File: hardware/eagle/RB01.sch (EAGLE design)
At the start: 10 parts, among them J1 CON_TERMINAL_BLOCK_03-5MM, J2 CON_TERMINAL_BLOCK_02-5MM, K1 JS-M1A-12V-5, Q1 BC547

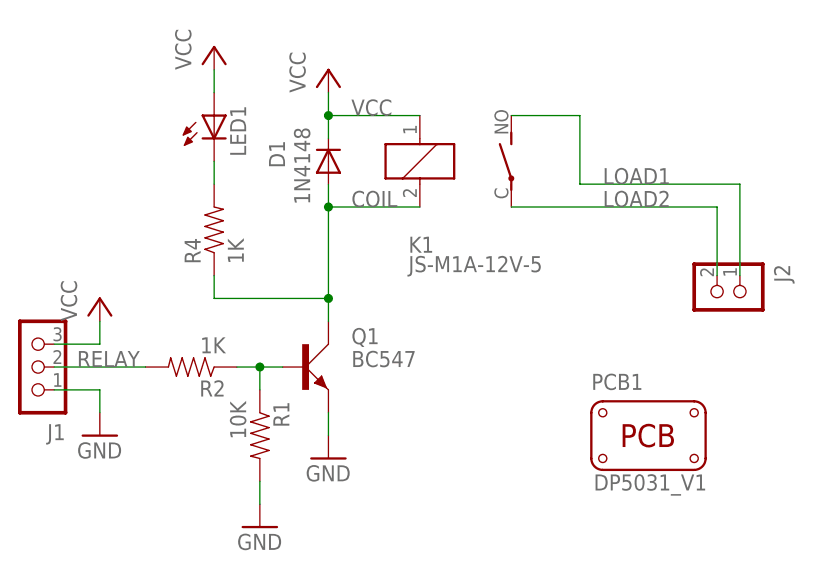
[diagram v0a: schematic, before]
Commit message: BC337s instead of BC546s
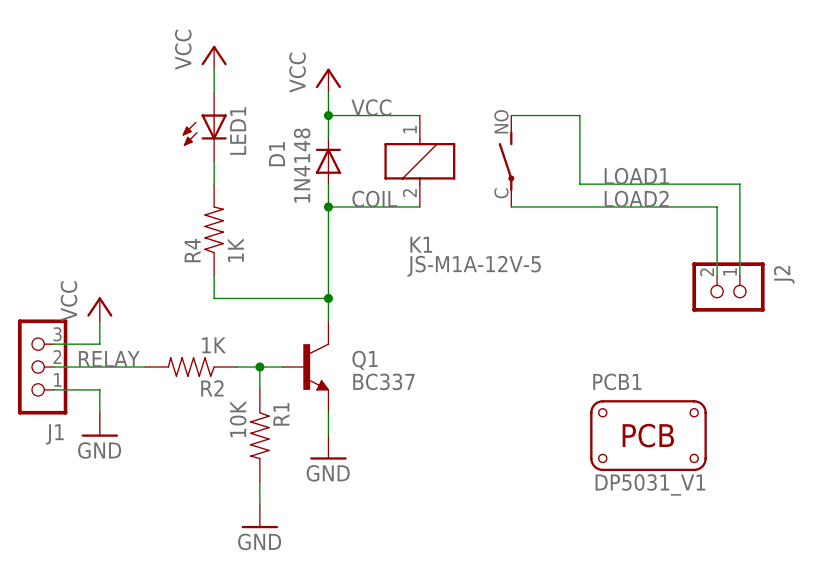
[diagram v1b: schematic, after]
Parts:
- Q1: value BC547 -> BC337; device transistor-small-signal:BC547 -> transistor:BC337
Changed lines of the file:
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@@
 <part name="J1" library="dp_devices" deviceset="CON_TERMINAL_BLOCK_03" device="-5MM"/>
 <part name="J2" library="dp_devices" deviceset="CON_TERMINAL_BLOCK_02" device="-5MM"/>
-<part name="Q1" library="transistor-small-signal" deviceset="BC547" device=""/>
+<part name="Q1" library="transistor" deviceset="BC337" device=""/>
 <part name="K1" library="relay" deviceset="JS-M1A*" device="" technology="-12V-5"/>
 <part name="PCB1" library="dp_devices" deviceset="PCB_DP_RECTANGLE" device="-31X50"/>
@@
 <instance part="J1" gate="CON" x="96.52" y="86.36" rot="R180"/>
 <instance part="J2" gate="CON" x="172.72" y="96.52" rot="R270"/>
-<instance part="Q1" gate="1" x="124.46" y="86.36"/>
+<instance part="Q1" gate="G$1" x="124.46" y="86.36" smashed="yes">
+<attribute name="NAME" x="129.54" y="86.36" size="1.778" layer="95"/>
+<attribute name="VALUE" x="129.54" y="83.82" size="1.778" layer="96"/>
+</instance>
 <instance part="K1" gate="1" x="137.16" y="109.22" smashed="yes">
 <attribute name="VALUE" x="135.89" y="96.901" size="1.778" layer="96"/>
@@
 <segment>
 <pinref part="GND1" gate="1" pin="GND"/>
-<pinref part="Q1" gate="1" pin="E"/>
+<pinref part="Q1" gate="G$1" pin="E"/>
 <wire x1="127" y1="78.74" x2="127" y2="81.28" width="0.1524" layer="91"/>
 </segment>
@@
 <pinref part="R2" gate="G$1" pin="1"/>
 <pinref part="R1" gate="G$1" pin="1"/>
-<pinref part="Q1" gate="1" pin="B"/>
+<pinref part="Q1" gate="G$1" pin="B"/>
 <wire x1="121.92" y1="86.36" x2="119.38" y2="86.36" width="0.1524" layer="91"/>
 <junction x="119.38" y="86.36"/>
@@
 <pinref part="D1" gate="G$1" pin="A"/>
 <pinref part="R4" gate="G$1" pin="1"/>
-<pinref part="Q1" gate="1" pin="C"/>
+<pinref part="Q1" gate="G$1" pin="C"/>
 <wire x1="127" y1="91.44" x2="127" y2="93.98" width="0.1524" layer="91"/>
 <junction x="127" y="93.98"/>

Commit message: JS-M1 relay package
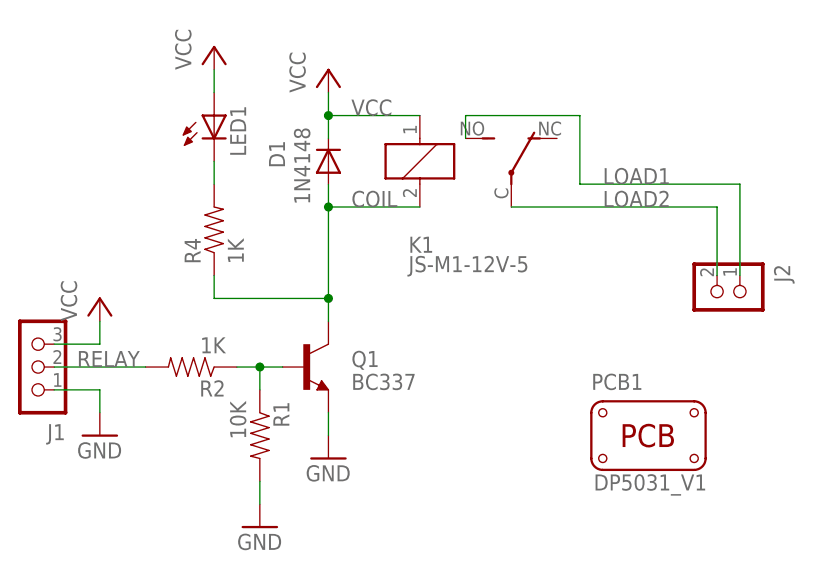
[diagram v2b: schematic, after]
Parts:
- K1: value JS-M1A-12V-5 -> JS-M1-12V-5; device relay:JS-M1A-12V-5 -> relay:JS-M1-12V-5; MF (none) -> FARNELL; MPN (none) -> JSM1-12V-5; OC_FARNELL (none) -> 910351; OC_NEWARK (none) -> 14J1764
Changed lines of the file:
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@@
 <part name="J2" library="dp_devices" deviceset="CON_TERMINAL_BLOCK_02" device="-5MM"/>
 <part name="Q1" library="transistor" deviceset="BC337" device=""/>
-<part name="K1" library="relay" deviceset="JS-M1A*" device="" technology="-12V-5"/>
+<part name="K1" library="relay" deviceset="JS-M1*" device="" technology="-12V-5">
+<attribute name="MF" value="FARNELL"/>
+<attribute name="MPN" value="JSM1-12V-5"/>
+<attribute name="OC_FARNELL" value="910351"/>
+<attribute name="OC_NEWARK" value="14J1764"/>
+</part>
 <part name="PCB1" library="dp_devices" deviceset="PCB_DP_RECTANGLE" device="-31X50"/>
 <part name="P+1" library="supply1" deviceset="VCC" device=""/>
@@
 <attribute name="PART" x="135.89" y="99.06" size="1.778" layer="95"/>
 </instance>
-<instance part="K1" gate="2" x="147.32" y="109.22" smashed="yes"/>
+<instance part="K1" gate="2" x="147.32" y="106.68" smashed="yes"/>
 <instance part="PCB1" gate="PCB" x="162.56" y="78.74"/>
 <instance part="P+1" gate="VCC" x="101.6" y="93.98"/>
@@
 <label x="157.48" y="106.68" size="1.778" layer="95"/>
 <pinref part="K1" gate="2" pin="S"/>
-<wire x1="147.32" y1="114.3" x2="154.94" y2="114.3" width="0.1524" layer="91"/>
+<wire x1="142.24" y1="111.76" x2="142.24" y2="114.3" width="0.1524" layer="91"/>
+<wire x1="142.24" y1="114.3" x2="154.94" y2="114.3" width="0.1524" layer="91"/>
 <wire x1="154.94" y1="114.3" x2="154.94" y2="106.68" width="0.1524" layer="91"/>
 <pinref part="J2" gate="CON" pin="1"/>
